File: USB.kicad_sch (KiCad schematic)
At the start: 4 parts, among them J1 USB_C_Receptacle_USB2.0_16P, U8 USBLC6-2SC6

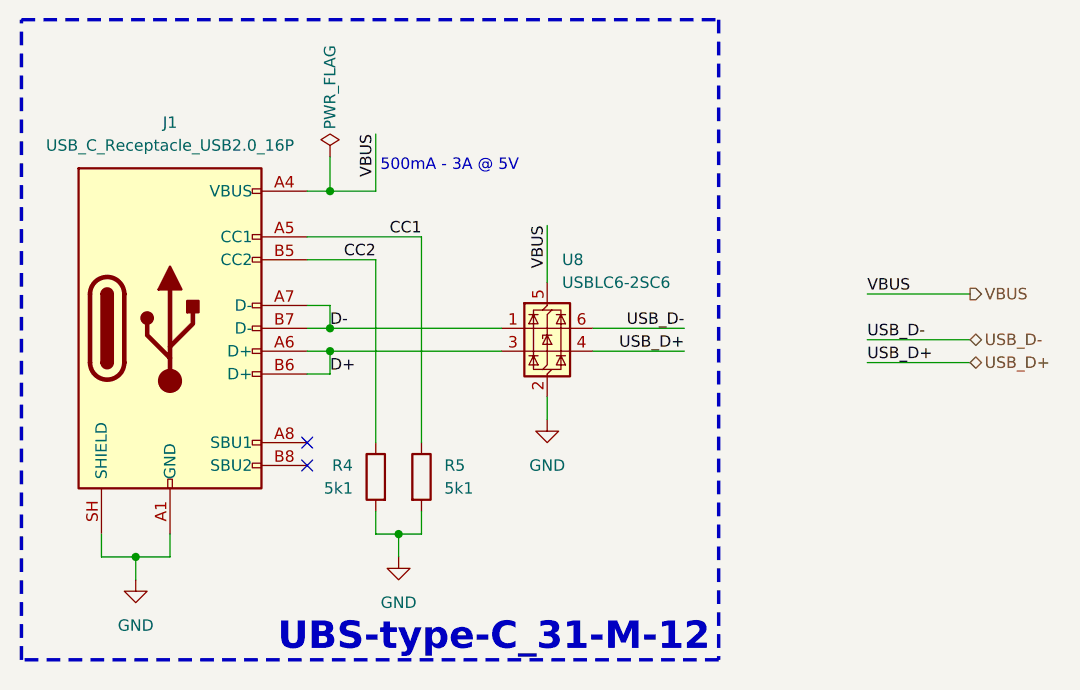
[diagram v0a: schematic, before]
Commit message: prep for chaneling. fixed the connector references, added cha to this schematic.
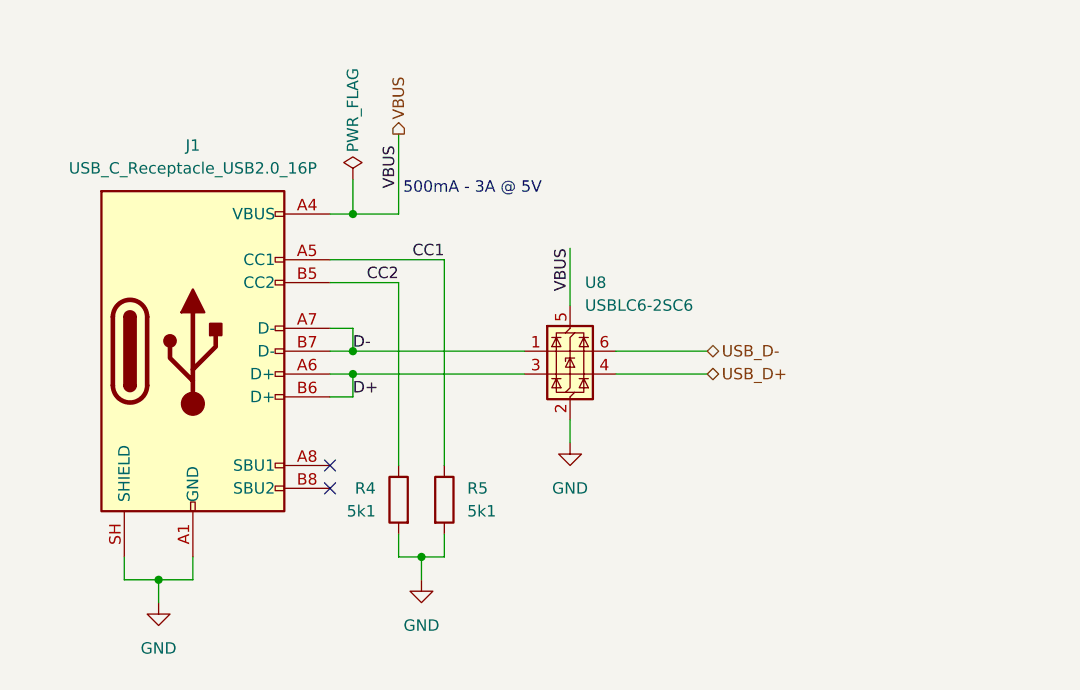
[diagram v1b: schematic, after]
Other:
- moved on the sheet: J1, R4, R5, U8

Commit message: more fixes for channels
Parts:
- renumbered J1 to J1001, R4 to R1027, R5 to R1028, U8 to U1006
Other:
- moved on the sheet: R1027, R1028
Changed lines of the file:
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@@
 	)
 	(junction
-		(at 147.32 110.49)
+		(at 147.32 114.3)
 		(diameter 0)
 		(color 0 0 0 0)
@@
 	(wire
 		(pts
-			(xy 144.78 110.49) (xy 144.78 107.95)
+			(xy 144.78 114.3) (xy 144.78 111.76)
 		)
 		(stroke
@@
 	(wire
 		(pts
-			(xy 147.32 110.49) (xy 147.32 113.03)
+			(xy 147.32 114.3) (xy 147.32 116.84)
 		)
 		(stroke
@@
 	(wire
 		(pts
-			(xy 149.86 77.47) (xy 149.86 100.33)
+			(xy 149.86 77.47) (xy 149.86 104.14)
 		)
 		(stroke
@@
 	(wire
 		(pts
-			(xy 147.32 110.49) (xy 144.78 110.49)
+			(xy 147.32 114.3) (xy 144.78 114.3)
 		)
 		(stroke
@@
 	(wire
 		(pts
-			(xy 149.86 107.95) (xy 149.86 110.49)
-		)
-		(stroke
-			(width 0)
-			(type default)
-		)
-	)
-	(wire
-		(pts
-			(xy 147.32 110.49) (xy 149.86 110.49)
+			(xy 149.86 111.76) (xy 149.86 114.3)
+		)
+		(stroke
+			(width 0)
+			(type default)
+		)
+	)
+	(wire
+		(pts
+			(xy 147.32 114.3) (xy 149.86 114.3)
 		)
 		(stroke
@@
 	(wire
 		(pts
-			(xy 144.78 100.33) (xy 144.78 80.01)
+			(xy 144.78 104.14) (xy 144.78 80.01)
 		)
 		(stroke
@@
 		(instances
 			(project "VESC6_OPEN_HARDWARE"
-				(path "/8bc2c25a-a1f1-4ce8-b96a-a4f8f4c35079/4c5fe8a6-8c75-4d28-a0d1-00076ab3fe22"
+				(path "/8bc2c25a-a1f1-4ce8-b96a-a4f8f4c35079/1e81ec4a-7813-42c9-8244-ecd5bd9e7dba/a8cef6d1-1c80-4870-a6aa-c1368869a3a7"
 					(reference "#PWR01")
-					(unit 1)
-				)
-			)
-			(project "UBS-C_TYPE-C-31-M-12"
-				(path "/d915b4b4-54fd-4193-8810-936621a064e8"
-					(reference "#PWR07")
 					(unit 1)
 				)
@@
 		(dnp no)
 		(fields_autoplaced yes)
-		(property "Reference" "U8"
+		(property "Reference" "U1006"
 			(at 165.4811 80.01 0)
 			(show_name no)
@@
 		(instances
 			(project "VESC6_OPEN_HARDWARE"
-				(path "/8bc2c25a-a1f1-4ce8-b96a-a4f8f4c35079/4c5fe8a6-8c75-4d28-a0d1-00076ab3fe22"
-					(reference "U8")
-					(unit 1)
-				)
-			)
-			(project "UBS-C_TYPE-C-31-M-12"
-				(path "/d915b4b4-54fd-4193-8810-936621a064e8"
-					(reference "U1")
+				(path "/8bc2c25a-a1f1-4ce8-b96a-a4f8f4c35079/1e81ec4a-7813-42c9-8244-ecd5bd9e7dba/a8cef6d1-1c80-4870-a6aa-c1368869a3a7"
+					(reference "U1006")
 					(unit 1)
 				)
@@
 		(instances
 			(project "VESC6_OPEN_HARDWARE"
-				(path "/8bc2c25a-a1f1-4ce8-b96a-a4f8f4c35079/4c5fe8a6-8c75-4d28-a0d1-00076ab3fe22"
+				(path "/8bc2c25a-a1f1-4ce8-b96a-a4f8f4c35079/1e81ec4a-7813-42c9-8244-ecd5bd9e7dba/a8cef6d1-1c80-4870-a6aa-c1368869a3a7"
 					(reference "#FLG01")
 					(unit 1)
 				)
 			)
-			(project "UBS-C_TYPE-C-31-M-12"
-				(path "/d915b4b4-54fd-4193-8810-936621a064e8"
-					(reference "#FLG01")
-					(unit 1)
-				)
-			)
 		)
 	)
 	(symbol
 		(lib_id "Device:R")
-		(at 149.86 104.14 0)
+		(at 149.86 107.95 0)
 		(unit 1)
 		(body_style 1)
@@
 		(in_pos_files yes)
 		(dnp no)
-		(property "Reference" "R5"
-			(at 152.4 102.8699 0)
+		(property "Reference" "R1028"
+			(at 152.4 106.6799 0)
 			(show_name no)
 			(do_not_autoplace no)
@@
 		)
 		(property "Value" "5k1"
-			(at 152.4 105.4099 0)
+			(at 152.4 109.2199 0)
 			(show_name no)
 			(do_not_autoplace no)
@@
 		)
 		(property "Footprint" "Resistor_SMD:R_0805_2012Metric_Pad1.20x1.40mm_HandSolder"
-			(at 148.082 104.14 90)
+			(at 148.082 107.95 90)
 			(hide yes)
 			(show_name no)
@@
 		)
 		(property "Datasheet" ""
-			(at 149.86 104.14 0)
+			(at 149.86 107.95 0)
 			(hide yes)
 			(show_name no)
@@
 		)
 		(property "Description" "Resistor"
-			(at 149.86 104.14 0)
+			(at 149.86 107.95 0)
 			(hide yes)
 			(show_name no)
@@
 		)
 		(property "LCSC" "C84375"
-			(at 149.86 104.14 0)
+			(at 149.86 107.95 0)
 			(hide yes)
 			(show_name no)
@@
 		(instances
 			(project "VESC6_OPEN_HARDWARE"
-				(path "/8bc2c25a-a1f1-4ce8-b96a-a4f8f4c35079/4c5fe8a6-8c75-4d28-a0d1-00076ab3fe22"
-					(reference "R5")
-					(unit 1)
-				)
-			)
-			(project "UBS-C_TYPE-C-31-M-12"
-				(path "/d915b4b4-54fd-4193-8810-936621a064e8"
-					(reference "R4")
+				(path "/8bc2c25a-a1f1-4ce8-b96a-a4f8f4c35079/1e81ec4a-7813-42c9-8244-ecd5bd9e7dba/a8cef6d1-1c80-4870-a6aa-c1368869a3a7"
+					(reference "R1028")
 					(unit 1)
 				)
@@
 		(dnp no)
 		(fields_autoplaced yes)
-		(property "Reference" "J1"
+		(property "Reference" "J1001"
 			(at 121.92 64.77 0)
 			(show_name no)
@@
 		(instances
 			(project "VESC6_OPEN_HARDWARE"
-				(path "/8bc2c25a-a1f1-4ce8-b96a-a4f8f4c35079/4c5fe8a6-8c75-4d28-a0d1-00076ab3fe22"
-					(reference "J1")
-					(unit 1)
-				)
-			)
-			(project "UBS-C_TYPE-C-31-M-12"
-				(path "/d915b4b4-54fd-4193-8810-936621a064e8"
-					(reference "J1")
+				(path "/8bc2c25a-a1f1-4ce8-b96a-a4f8f4c35079/1e81ec4a-7813-42c9-8244-ecd5bd9e7dba/a8cef6d1-1c80-4870-a6aa-c1368869a3a7"
+					(reference "J1001")
 					(unit 1)
 				)
@@
 	(symbol
 		(lib_id "power:GND")
-		(at 147.32 113.03 0)
+		(at 147.32 116.84 0)
 		(unit 1)
 		(body_style 1)
@@
 		(fields_autoplaced yes)
 		(property "Reference" "#PWR03"
-			(at 147.32 119.38 0)
+			(at 147.32 123.19 0)
 			(hide yes)
 			(show_name no)
@@
 		)
 		(property "Value" "GND"
-			(at 147.32 118.11 0)
+			(at 147.32 121.92 0)
 			(show_name no)
 			(do_not_autoplace no)
@@
 		)
 		(property "Footprint" ""
-			(at 147.32 113.03 0)
+			(at 147.32 116.84 0)
 			(hide yes)
 			(show_name no)
@@
 		)
 		(property "Datasheet" ""
-			(at 147.32 113.03 0)
+			(at 147.32 116.84 0)
 			(hide yes)
 			(show_name no)
@@
 		)
 		(property "Description" "Power symbol creates a global label with name \"GND\" , ground"
-			(at 147.32 113.03 0)
+			(at 147.32 116.84 0)
 			(hide yes)
 			(show_name no)
@@
 		(instances
 			(project "VESC6_OPEN_HARDWARE"
-				(path "/8bc2c25a-a1f1-4ce8-b96a-a4f8f4c35079/4c5fe8a6-8c75-4d28-a0d1-00076ab3fe22"
+				(path "/8bc2c25a-a1f1-4ce8-b96a-a4f8f4c35079/1e81ec4a-7813-42c9-8244-ecd5bd9e7dba/a8cef6d1-1c80-4870-a6aa-c1368869a3a7"
 					(reference "#PWR03")
-					(unit 1)
-				)
-			)
-			(project "UBS-C_TYPE-C-31-M-12"
-				(path "/d915b4b4-54fd-4193-8810-936621a064e8"
-					(reference "#PWR08")
 					(unit 1)
 				)
@@
 		(instances
 			(project "VESC6_OPEN_HARDWARE"
-				(path "/8bc2c25a-a1f1-4ce8-b96a-a4f8f4c35079/4c5fe8a6-8c75-4d28-a0d1-00076ab3fe22"
+				(path "/8bc2c25a-a1f1-4ce8-b96a-a4f8f4c35079/1e81ec4a-7813-42c9-8244-ecd5bd9e7dba/a8cef6d1-1c80-4870-a6aa-c1368869a3a7"
 					(reference "#PWR08")
 					(unit 1)
 				)
 			)
-			(project "UBS-C_TYPE-C-31-M-12"
-				(path "/d915b4b4-54fd-4193-8810-936621a064e8"
-					(reference "#PWR09")
-					(unit 1)
-				)
-			)
 		)
 	)
 	(symbol
 		(lib_id "Device:R")
-		(at 144.78 104.14 0)
+		(at 144.78 107.95 0)
 		(mirror y)
 		(unit 1)
@@
 		(in_pos_files yes)
 		(dnp no)
-		(property "Reference" "R4"
-			(at 142.24 102.8699 0)
+		(property "Reference" "R1027"
+			(at 142.24 106.6799 0)
 			(show_name no)
 			(do_not_autoplace no)
@@
 		)
 		(property "Value" "5k1"
-			(at 142.24 105.4099 0)
+			(at 142.24 109.2199 0)
 			(show_name no)
 			(do_not_autoplace no)
@@
 		)
 		(property "Footprint" "Resistor_SMD:R_0805_2012Metric_Pad1.20x1.40mm_HandSolder"
-			(at 146.558 104.14 90)
+			(at 146.558 107.95 90)
 			(hide yes)
 			(show_name no)
@@
 		)
 		(property "Datasheet" ""
-			(at 144.78 104.14 0)
+			(at 144.78 107.95 0)
 			(hide yes)
 			(show_name no)
@@
 		)
 		(property "Description" "Resistor"
-			(at 144.78 104.14 0)
+			(at 144.78 107.95 0)
 			(hide yes)
 			(show_name no)
@@
 		)
 		(property "LCSC" "C84375"
-			(at 144.78 104.14 0)
+			(at 144.78 107.95 0)
 			(hide yes)
 			(show_name no)
@@
 		(instances
 			(project "VESC6_OPEN_HARDWARE"
-				(path "/8bc2c25a-a1f1-4ce8-b96a-a4f8f4c35079/4c5fe8a6-8c75-4d28-a0d1-00076ab3fe22"
-					(reference "R4")
+				(path "/8bc2c25a-a1f1-4ce8-b96a-a4f8f4c35079/1e81ec4a-7813-42c9-8244-ecd5bd9e7dba/a8cef6d1-1c80-4870-a6aa-c1368869a3a7"
+					(reference "R1027")
 					(unit 1)
 				)
-			)
-			(project "UBS-C_TYPE-C-31-M-12"
-				(path "/d915b4b4-54fd-4193-8810-936621a064e8"
-					(reference "R5")
-					(unit 1)
-				)

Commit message: relinked UUIDs
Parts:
- renumbered J1001 to J101, R1027 to R132, R1028 to R133, U1006 to U108
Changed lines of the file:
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@@
 		(dnp no)
 		(fields_autoplaced yes)
-		(property "Reference" "U1006"
+		(property "Reference" "U108"
 			(at 165.4811 80.01 0)
 			(show_name no)
@@
 			(project "VESC6_OPEN_HARDWARE"
 				(path "/8bc2c25a-a1f1-4ce8-b96a-a4f8f4c35079/1e81ec4a-7813-42c9-8244-ecd5bd9e7dba/a8cef6d1-1c80-4870-a6aa-c1368869a3a7"
-					(reference "U1006")
+					(reference "U108")
 					(unit 1)
 				)
@@
 		(in_pos_files yes)
 		(dnp no)
-		(property "Reference" "R1028"
+		(property "Reference" "R133"
 			(at 152.4 106.6799 0)
 			(show_name no)
@@
 			(project "VESC6_OPEN_HARDWARE"
 				(path "/8bc2c25a-a1f1-4ce8-b96a-a4f8f4c35079/1e81ec4a-7813-42c9-8244-ecd5bd9e7dba/a8cef6d1-1c80-4870-a6aa-c1368869a3a7"
-					(reference "R1028")
+					(reference "R133")
 					(unit 1)
 				)
@@
 		(dnp no)
 		(fields_autoplaced yes)
-		(property "Reference" "J1001"
+		(property "Reference" "J101"
 			(at 121.92 64.77 0)
 			(show_name no)
@@
 			(project "VESC6_OPEN_HARDWARE"
 				(path "/8bc2c25a-a1f1-4ce8-b96a-a4f8f4c35079/1e81ec4a-7813-42c9-8244-ecd5bd9e7dba/a8cef6d1-1c80-4870-a6aa-c1368869a3a7"
-					(reference "J1001")
+					(reference "J101")
 					(unit 1)
 				)
@@
 		(in_pos_files yes)
 		(dnp no)
-		(property "Reference" "R1027"
+		(property "Reference" "R132"
 			(at 142.24 106.6799 0)
 			(show_name no)
@@
 			(project "VESC6_OPEN_HARDWARE"
 				(path "/8bc2c25a-a1f1-4ce8-b96a-a4f8f4c35079/1e81ec4a-7813-42c9-8244-ecd5bd9e7dba/a8cef6d1-1c80-4870-a6aa-c1368869a3a7"
-					(reference "R1027")
+					(reference "R132")
 					(unit 1)
 				)

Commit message: it seems to work. yay
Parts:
- renumbered J101 to J1401, R132 to R1401, R133 to R1402, U108 to U1401
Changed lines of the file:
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@@
 		(dnp no)
 		(fields_autoplaced yes)
-		(property "Reference" "#PWR01"
+		(property "Reference" "#PWR01401"
 			(at 118.11 121.92 0)
 			(hide yes)
@@
 			(project "VESC6_OPEN_HARDWARE"
 				(path "/8bc2c25a-a1f1-4ce8-b96a-a4f8f4c35079/1e81ec4a-7813-42c9-8244-ecd5bd9e7dba/a8cef6d1-1c80-4870-a6aa-c1368869a3a7"
-					(reference "#PWR01")
+					(reference "#PWR01401")
+					(unit 1)
+				)
+				(path "/8bc2c25a-a1f1-4ce8-b96a-a4f8f4c35079/cc03c9bc-7d6e-4340-8742-d977d081ffa4/91b402ab-9ee1-47ae-a39a-545f22c082a7"
+					(reference "#PWR02401")
 					(unit 1)
 				)
@@
 		(dnp no)
 		(fields_autoplaced yes)
-		(property "Reference" "U108"
+		(property "Reference" "U1401"
 			(at 165.4811 80.01 0)
 			(show_name no)
@@
 			(project "VESC6_OPEN_HARDWARE"
 				(path "/8bc2c25a-a1f1-4ce8-b96a-a4f8f4c35079/1e81ec4a-7813-42c9-8244-ecd5bd9e7dba/a8cef6d1-1c80-4870-a6aa-c1368869a3a7"
-					(reference "U108")
+					(reference "U1401")
+					(unit 1)
+				)
+				(path "/8bc2c25a-a1f1-4ce8-b96a-a4f8f4c35079/cc03c9bc-7d6e-4340-8742-d977d081ffa4/91b402ab-9ee1-47ae-a39a-545f22c082a7"
+					(reference "U2401")
 					(unit 1)
 				)
@@
 		(in_pos_files yes)
 		(dnp no)
-		(property "Reference" "#FLG01"
+		(property "Reference" "#FLG01401"
 			(at 139.7 66.675 0)
 			(hide yes)
@@
 			(project "VESC6_OPEN_HARDWARE"
 				(path "/8bc2c25a-a1f1-4ce8-b96a-a4f8f4c35079/1e81ec4a-7813-42c9-8244-ecd5bd9e7dba/a8cef6d1-1c80-4870-a6aa-c1368869a3a7"
-					(reference "#FLG01")
+					(reference "#FLG01401")
+					(unit 1)
+				)
+				(path "/8bc2c25a-a1f1-4ce8-b96a-a4f8f4c35079/cc03c9bc-7d6e-4340-8742-d977d081ffa4/91b402ab-9ee1-47ae-a39a-545f22c082a7"
+					(reference "#FLG02401")
 					(unit 1)
 				)
@@
 		(in_pos_files yes)
 		(dnp no)
-		(property "Reference" "R133"
+		(property "Reference" "R1402"
 			(at 152.4 106.6799 0)
 			(show_name no)
@@
 			(project "VESC6_OPEN_HARDWARE"
 				(path "/8bc2c25a-a1f1-4ce8-b96a-a4f8f4c35079/1e81ec4a-7813-42c9-8244-ecd5bd9e7dba/a8cef6d1-1c80-4870-a6aa-c1368869a3a7"
-					(reference "R133")
+					(reference "R1402")
+					(unit 1)
+				)
+				(path "/8bc2c25a-a1f1-4ce8-b96a-a4f8f4c35079/cc03c9bc-7d6e-4340-8742-d977d081ffa4/91b402ab-9ee1-47ae-a39a-545f22c082a7"
+					(reference "R2402")
 					(unit 1)
 				)
@@
 		(dnp no)
 		(fields_autoplaced yes)
-		(property "Reference" "J101"
+		(property "Reference" "J1401"
 			(at 121.92 64.77 0)
 			(show_name no)
@@
 			(project "VESC6_OPEN_HARDWARE"
 				(path "/8bc2c25a-a1f1-4ce8-b96a-a4f8f4c35079/1e81ec4a-7813-42c9-8244-ecd5bd9e7dba/a8cef6d1-1c80-4870-a6aa-c1368869a3a7"
-					(reference "J101")
+					(reference "J1401")
+					(unit 1)
+				)
+				(path "/8bc2c25a-a1f1-4ce8-b96a-a4f8f4c35079/cc03c9bc-7d6e-4340-8742-d977d081ffa4/91b402ab-9ee1-47ae-a39a-545f22c082a7"
+					(reference "J2401")
 					(unit 1)
 				)
@@
 		(dnp no)
 		(fields_autoplaced yes)
-		(property "Reference" "#PWR03"
+		(property "Reference" "#PWR01402"
 			(at 147.32 123.19 0)
 			(hide yes)
@@
 			(project "VESC6_OPEN_HARDWARE"
 				(path "/8bc2c25a-a1f1-4ce8-b96a-a4f8f4c35079/1e81ec4a-7813-42c9-8244-ecd5bd9e7dba/a8cef6d1-1c80-4870-a6aa-c1368869a3a7"
-					(reference "#PWR03")
+					(reference "#PWR01402")
+					(unit 1)
+				)
+				(path "/8bc2c25a-a1f1-4ce8-b96a-a4f8f4c35079/cc03c9bc-7d6e-4340-8742-d977d081ffa4/91b402ab-9ee1-47ae-a39a-545f22c082a7"
+					(reference "#PWR02402")
 					(unit 1)
 				)
@@
 		(dnp no)
 		(fields_autoplaced yes)
-		(property "Reference" "#PWR08"
+		(property "Reference" "#PWR01403"
 			(at 163.83 104.14 0)
 			(hide yes)
@@
 			(project "VESC6_OPEN_HARDWARE"
 				(path "/8bc2c25a-a1f1-4ce8-b96a-a4f8f4c35079/1e81ec4a-7813-42c9-8244-ecd5bd9e7dba/a8cef6d1-1c80-4870-a6aa-c1368869a3a7"
-					(reference "#PWR08")
+					(reference "#PWR01403")
+					(unit 1)
+				)
+				(path "/8bc2c25a-a1f1-4ce8-b96a-a4f8f4c35079/cc03c9bc-7d6e-4340-8742-d977d081ffa4/91b402ab-9ee1-47ae-a39a-545f22c082a7"
+					(reference "#PWR02403")
 					(unit 1)
 				)
@@
 		(in_pos_files yes)
 		(dnp no)
-		(property "Reference" "R132"
+		(property "Reference" "R1401"
 			(at 142.24 106.6799 0)
 			(show_name no)
@@
 			(project "VESC6_OPEN_HARDWARE"
 				(path "/8bc2c25a-a1f1-4ce8-b96a-a4f8f4c35079/1e81ec4a-7813-42c9-8244-ecd5bd9e7dba/a8cef6d1-1c80-4870-a6aa-c1368869a3a7"
-					(reference "R132")
-					(unit 1)
-				)
+					(reference "R1401")
+					(unit 1)
+				)
+				(path "/8bc2c25a-a1f1-4ce8-b96a-a4f8f4c35079/cc03c9bc-7d6e-4340-8742-d977d081ffa4/91b402ab-9ee1-47ae-a39a-545f22c082a7"
+					(reference "R2401")
+					(unit 1)
+				)

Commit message: more tweaks
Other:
- company: (none) -> craigg96, Tomáš Kuchta
- title: (none) -> 2ch VESC based on VESC6
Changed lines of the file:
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@@
 	(paper "A4")
 	(title_block
-		(rev "A")
+		(title "2ch VESC based on VESC6")
+		(rev "B")
+		(company "craigg96, Tomáš Kuchta")
 	)
 	(text "500mA - 3A @ 5V"
